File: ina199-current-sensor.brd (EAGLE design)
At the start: 10.8 x 17.1 mm, 9 parts

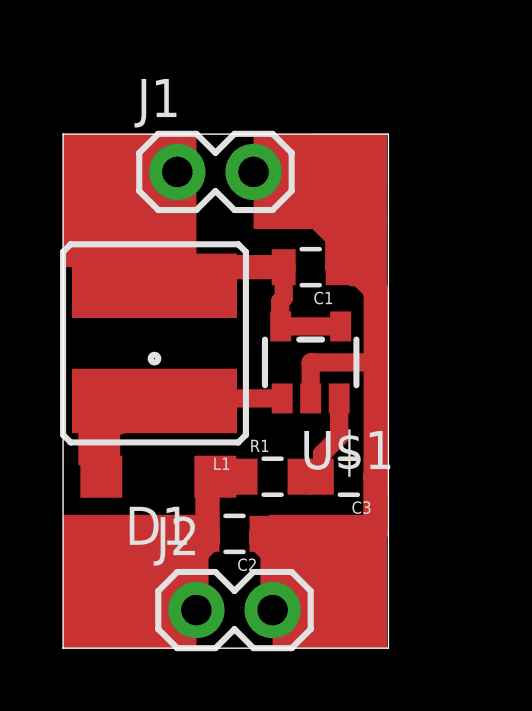
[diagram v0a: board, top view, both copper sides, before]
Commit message: Modified board layouts
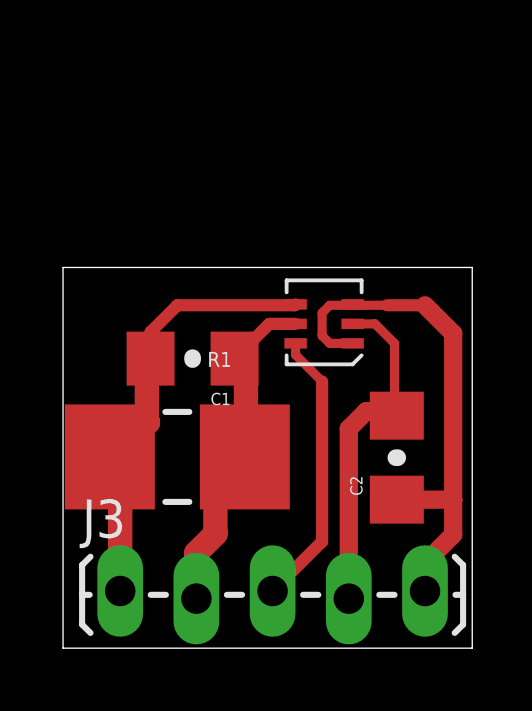
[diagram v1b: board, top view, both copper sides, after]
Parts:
- removed C3: 1uF, SparkFun:0805
- removed D1: MBR0520, diode:SOD123
- removed J1, J2: (no value), SparkFun-Connectors:1X02
- removed L1: 22uH, SparkFun:CR54
- added J3: (no value), SparkFun-Connectors:1X05_LOCK_LONGPADS
- C1, C2: value 100uF -> 1.0uF; device SparkFun:0805 -> SparkFun-Capacitors:1206-CAP
- R1: value 10 -> 0.001; device SparkFun-Resistors:0805 -> SparkFun-Resistors:2512
- U$1: value SP6641B -> INA199SC70; device Sipex Custom:SOT23-5 -> Synapseware:SC70-6
- moved C2 5.98 mm to (11.1, 6.35), turned to 90 degrees
- moved C1 4.98 mm to (4.32, 9.65)
- moved R1 3.24 mm to (3.81, 6.38)
- moved U$1 1.53 mm to (9.65, 10.2), turned to 90 degrees
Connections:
- removed net N$1: C3.2, R1.2, U$1.3
- removed net N$3: D1.A, L1.P$1, U$1.1
- removed net VBATT: C1.2, J1.1, L1.P$2, U$1.4, U$1.5
- removed net VOUT: C2.2, D1.C, J2.1, R1.1
- new net 5V: C2.1, J3.5, U$1.1, U$1.3
- new net LOAD: C1.1, J3.2, R1.2, U$1.5
- new net OUT: J3.3, U$1.6
- new net SUPPLY: C1.2, J3.1, R1.1, U$1.4
- net GND: now also C2.2, J3.4; no longer C1.1, C2.1, C3.1, J1.2, J2.2
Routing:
- net 5V: track 0.00 -> 17.6 mm
- net SUPPLY: track 0.00 -> 14.8 mm
- net VBATT: track 13.7 -> 0.00 mm
- net GND: track 25.0 -> 12.1 mm
- net LOAD: track 0.00 -> 12.9 mm
- net N$3: track 9.55 -> 0.00 mm
- net OUT: track 0.00 -> 9.31 mm
- net VOUT: track 4.71 -> 0.00 mm
- net N$1: track 2.85 -> 0.00 mm
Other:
- board size 10.8 x 17.1 mm -> 13.6 x 12.7 mm
